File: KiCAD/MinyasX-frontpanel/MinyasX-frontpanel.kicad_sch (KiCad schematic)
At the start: 30 parts, among them J101 Conn_01x04, J102 Conn_02x06_Odd_Even, SW101 SW_Push, SW102 SW_Push, U101 SLG46826G(V2), U102 JOYSTICK, U17 XC6201P332MR-G, U22 PCA9515DP

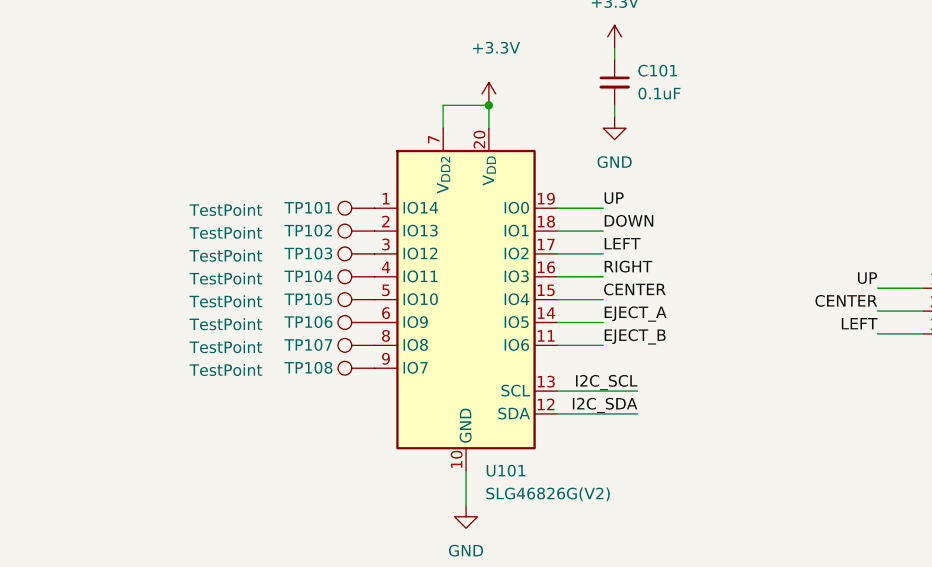
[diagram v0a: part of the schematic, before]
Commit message: * フロントパネルのキー操作ができるようにした * 画面のページ切り替えができるようにした * FDDの回転数とbpsの推定コードを修正した
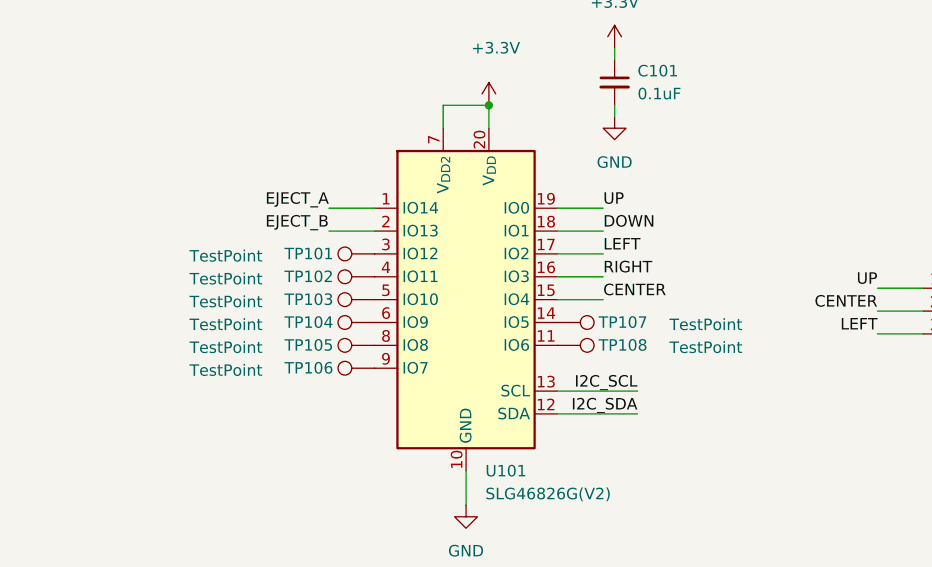
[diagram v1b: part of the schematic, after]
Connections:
- net EJECT_A: now also U101.1 (IO14); no longer U101.14 (IO5)
- net EJECT_B: now also U101.2 (IO13); no longer U101.11 (IO6)
- net at TP106.1: now also U101.9 (IO7); no longer U101.6 (IO9)
- net at TP103.1: now also U101.5 (IO10); no longer U101.3 (IO12)
- net at TP102.1: now also U101.4 (IO11); no longer U101.2 (IO13)
- net at TP107.1: now also U101.14 (IO5); no longer U101.8 (IO8)
- net at TP101.1: now also U101.3 (IO12); no longer U101.1 (IO14)
- net at TP104.1: now also U101.6 (IO9); no longer U101.4 (IO11)
- net at TP105.1: now also U101.8 (IO8); no longer U101.5 (IO10)
- net at TP108.1: now also U101.11 (IO6); no longer U101.9 (IO7)
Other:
- moved on the sheet: TP101, TP102, TP103, TP104, TP105, TP106, TP107, TP108
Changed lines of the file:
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@@
 	(wire
 		(pts
-			(xy 111.76 129.54) (xy 106.68 129.54)
+			(xy 81.28 116.84) (xy 86.36 116.84)
 		)
 		(stroke
@@
 	(wire
 		(pts
-			(xy 111.76 132.08) (xy 106.68 132.08)
+			(xy 81.28 119.38) (xy 86.36 119.38)
 		)
 		(stroke
@@
 	)
 	(label "EJECT_B"
-		(at 111.76 132.08 0)
+		(at 81.28 119.38 180)
 		(effects
 			(font
 				(size 1.27 1.27)
 			)
-			(justify left bottom)
+			(justify right bottom)
 		)
 	)
@@
 	)
 	(label "EJECT_A"
-		(at 111.76 129.54 0)
+		(at 81.28 116.84 180)
 		(effects
 			(font
 				(size 1.27 1.27)
 			)
-			(justify left bottom)
+			(justify right bottom)
 		)
 	)
@@
 	(symbol
 		(lib_id "Connector:TestPoint")
-		(at 86.36 129.54 90)
+		(at 86.36 134.62 90)
 		(unit 1)
 		(exclude_from_sim no)
@@
 		(dnp no)
 		(property "Reference" "TP106"
-			(at 81.788 129.54 90)
+			(at 81.788 134.62 90)
 			(effects
 				(font
@@
 		)
 		(property "Value" "TestPoint"
-			(at 73.914 129.794 90)
+			(at 73.914 134.874 90)
 			(effects
 				(font
@@
 		)
 		(property "Footprint" "TestPoint:TestPoint_Pad_1.0x1.0mm"
-			(at 86.36 124.46 0)
+			(at 86.36 129.54 0)
 			(effects
 				(font
@@
 		)
 		(property "Datasheet" "~"
-			(at 86.36 124.46 0)
+			(at 86.36 129.54 0)
 			(effects
 				(font
@@
 		)
 		(property "Description" "test point"
-			(at 86.36 129.54 0)
+			(at 86.36 134.62 0)
 			(effects
 				(font
@@
 	(symbol
 		(lib_id "Connector:TestPoint")
-		(at 86.36 121.92 90)
+		(at 86.36 127 90)
 		(unit 1)
 		(exclude_from_sim no)
@@
 		(dnp no)
 		(property "Reference" "TP103"
-			(at 81.788 121.92 90)
+			(at 81.788 127 90)
 			(effects
 				(font
@@
 		)
 		(property "Value" "TestPoint"
-			(at 73.914 122.174 90)
+			(at 73.914 127.254 90)
 			(effects
 				(font
@@
 		)
 		(property "Footprint" "TestPoint:TestPoint_Pad_1.0x1.0mm"
-			(at 86.36 116.84 0)
+			(at 86.36 121.92 0)
 			(effects
 				(font
@@
 		)
 		(property "Datasheet" "~"
-			(at 86.36 116.84 0)
+			(at 86.36 121.92 0)
 			(effects
 				(font
@@
 		)
 		(property "Description" "test point"
-			(at 86.36 121.92 0)
+			(at 86.36 127 0)
 			(effects
 				(font
@@
 	(symbol
 		(lib_id "Connector:TestPoint")
-		(at 86.36 119.38 90)
+		(at 86.36 124.46 90)
 		(unit 1)
 		(exclude_from_sim no)
@@
 		(dnp no)
 		(property "Reference" "TP102"
-			(at 81.788 119.38 90)
+			(at 81.788 124.46 90)
 			(effects
 				(font
@@
 		)
 		(property "Value" "TestPoint"
-			(at 73.914 119.634 90)
+			(at 73.914 124.714 90)
 			(effects
 				(font
@@
 		)
 		(property "Footprint" "TestPoint:TestPoint_Pad_1.0x1.0mm"
-			(at 86.36 114.3 0)
+			(at 86.36 119.38 0)
 			(effects
 				(font
@@
 		)
 		(property "Datasheet" "~"
-			(at 86.36 114.3 0)
+			(at 86.36 119.38 0)
 			(effects
 				(font
@@
 		)
 		(property "Description" "test point"
-			(at 86.36 119.38 0)
+			(at 86.36 124.46 0)
 			(effects
 				(font
@@
 	(symbol
 		(lib_id "Connector:TestPoint")
-		(at 86.36 132.08 90)
+		(at 106.68 129.54 270)
+		(mirror x)
 		(unit 1)
 		(exclude_from_sim no)
@@
 		(dnp no)
 		(property "Reference" "TP107"
-			(at 81.788 132.08 90)
+			(at 111.252 129.54 90)
 			(effects
 				(font
@@
 		)
 		(property "Value" "TestPoint"
-			(at 73.914 132.334 90)
+			(at 119.126 129.794 90)
 			(effects
 				(font
@@
 		)
 		(property "Footprint" "TestPoint:TestPoint_Pad_1.0x1.0mm"
-			(at 86.36 127 0)
+			(at 106.68 124.46 0)
 			(effects
 				(font
@@
 		)
 		(property "Datasheet" "~"
-			(at 86.36 127 0)
+			(at 106.68 124.46 0)
 			(effects
 				(font
@@
 		)
 		(property "Description" "test point"
-			(at 86.36 132.08 0)
+			(at 106.68 129.54 0)
 			(effects
 				(font
@@
 	(symbol
 		(lib_id "Connector:TestPoint")
-		(at 86.36 116.84 90)
+		(at 86.36 121.92 90)
 		(unit 1)
 		(exclude_from_sim no)
@@
 		(dnp no)
 		(property "Reference" "TP101"
-			(at 81.788 116.84 90)
+			(at 81.788 121.92 90)
 			(effects
 				(font
@@
 		)
 		(property "Value" "TestPoint"
-			(at 73.914 117.094 90)
+			(at 73.914 122.174 90)
 			(effects
 				(font
@@
 		)
 		(property "Footprint" "TestPoint:TestPoint_Pad_1.0x1.0mm"
-			(at 86.36 111.76 0)
+			(at 86.36 116.84 0)
 			(effects
 				(font
@@
 		)
 		(property "Datasheet" "~"
-			(at 86.36 111.76 0)
+			(at 86.36 116.84 0)
 			(effects
 				(font
@@
 		)
 		(property "Description" "test point"
-			(at 86.36 116.84 0)
+			(at 86.36 121.92 0)
 			(effects
 				(font
@@
 	(symbol
 		(lib_id "Connector:TestPoint")
-		(at 86.36 124.46 90)
+		(at 86.36 129.54 90)
 		(unit 1)
 		(exclude_from_sim no)
@@
 		(dnp no)
 		(property "Reference" "TP104"
-			(at 81.788 124.46 90)
+			(at 81.788 129.54 90)
 			(effects
 				(font
@@
 		)
 		(property "Value" "TestPoint"
-			(at 73.914 124.714 90)
+			(at 73.914 129.794 90)
 			(effects
 				(font
@@
 		)
 		(property "Footprint" "TestPoint:TestPoint_Pad_1.0x1.0mm"
-			(at 86.36 119.38 0)
+			(at 86.36 124.46 0)
 			(effects
 				(font
@@
 		)
 		(property "Datasheet" "~"
-			(at 86.36 119.38 0)
+			(at 86.36 124.46 0)
 			(effects
 				(font
@@
 		)
 		(property "Description" "test point"
-			(at 86.36 124.46 0)
+			(at 86.36 129.54 0)
 			(effects
 				(font
@@
 	(symbol
 		(lib_id "Connector:TestPoint")
-		(at 86.36 134.62 90)
+		(at 106.68 132.08 270)
+		(mirror x)
 		(unit 1)
 		(exclude_from_sim no)
@@
 		(dnp no)
 		(property "Reference" "TP108"
-			(at 81.788 134.62 90)
+			(at 111.252 132.08 90)
 			(effects
 				(font
@@
 		)
 		(property "Value" "TestPoint"
-			(at 73.914 134.874 90)
+			(at 119.126 132.334 90)
 			(effects
 				(font
@@
 		)
 		(property "Footprint" "TestPoint:TestPoint_Pad_1.0x1.0mm"
-			(at 86.36 129.54 0)
+			(at 106.68 127 0)
 			(effects
 				(font
@@
 		)
 		(property "Datasheet" "~"
-			(at 86.36 129.54 0)
+			(at 106.68 127 0)
 			(effects
 				(font
@@
 		)
 		(property "Description" "test point"
-			(at 86.36 134.62 0)
+			(at 106.68 132.08 0)
 			(effects
 				(font
@@
 	(symbol
 		(lib_id "Connector:TestPoint")
-		(at 86.36 127 90)
+		(at 86.36 132.08 90)
 		(unit 1)
 		(exclude_from_sim no)
@@
 		(dnp no)
 		(property "Reference" "TP105"
-			(at 81.788 127 90)
+			(at 81.788 132.08 90)
 			(effects
 				(font
@@
 		)
 		(property "Value" "TestPoint"
-			(at 73.914 127.254 90)
+			(at 73.914 132.334 90)
 			(effects
 				(font
@@
 		)
 		(property "Footprint" "TestPoint:TestPoint_Pad_1.0x1.0mm"
-			(at 86.36 121.92 0)
+			(at 86.36 127 0)
 			(effects
 				(font
@@
 		)
 		(property "Datasheet" "~"
-			(at 86.36 121.92 0)
+			(at 86.36 127 0)
 			(effects
 				(font
@@
 		)
 		(property "Description" "test point"
-			(at 86.36 127 0)
+			(at 86.36 132.08 0)
 			(effects
 				(font

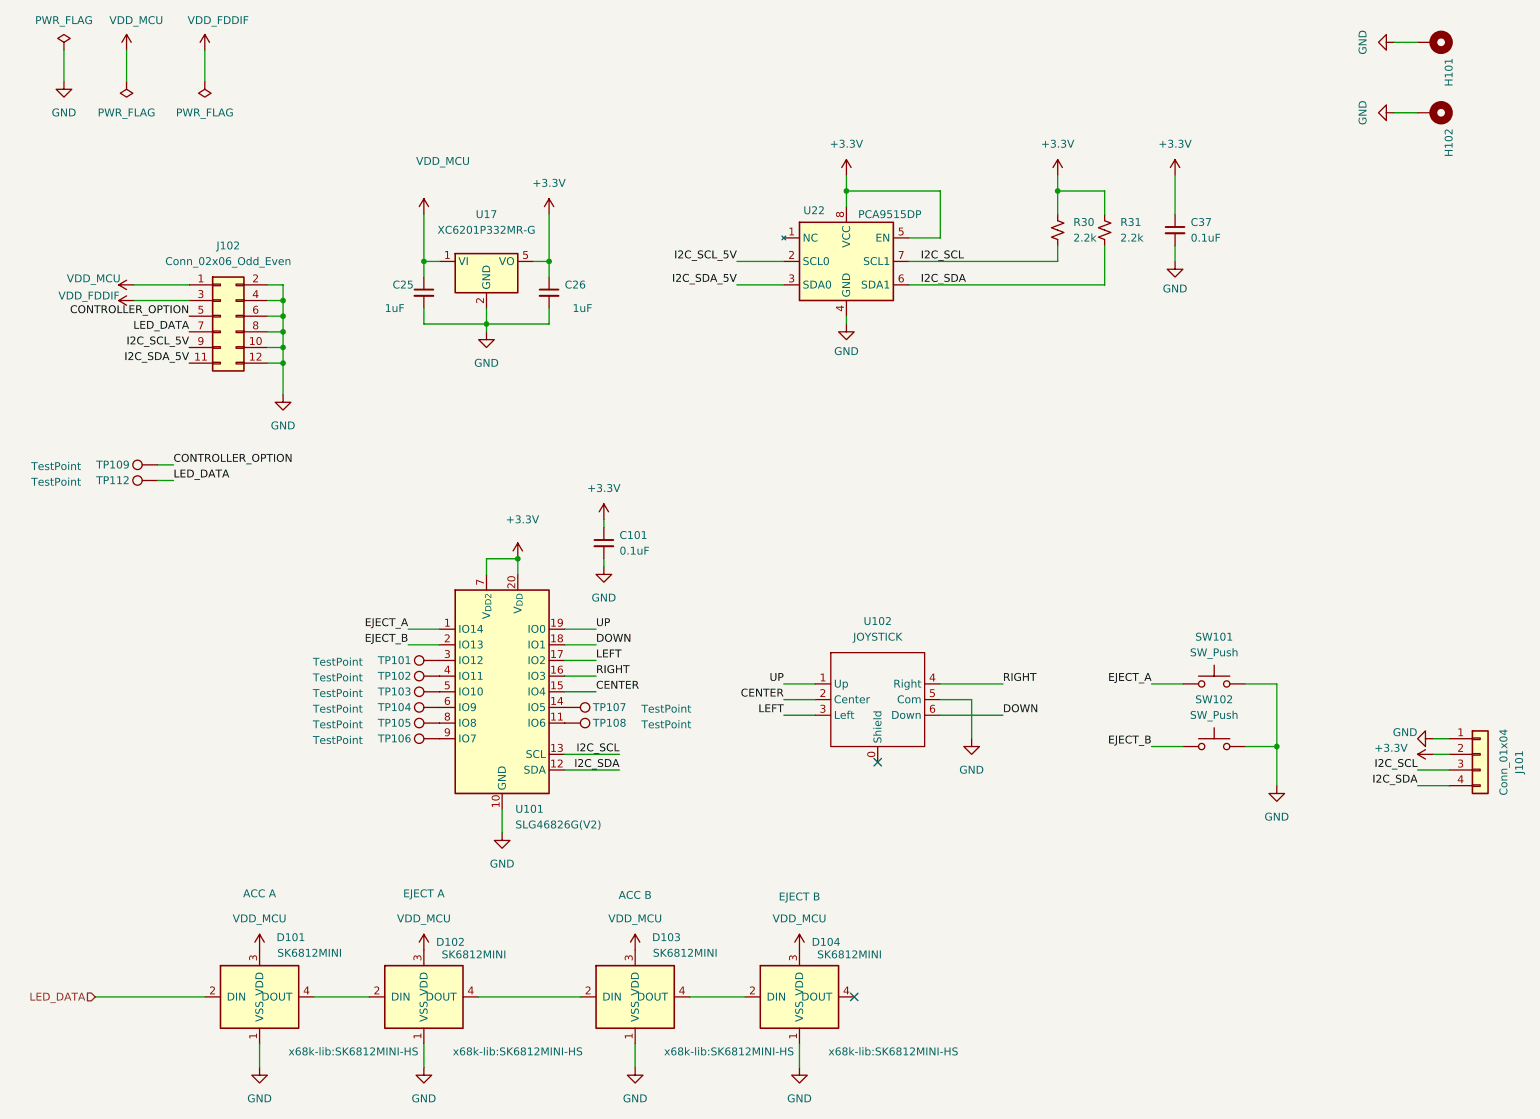
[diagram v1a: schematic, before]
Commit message: フロントパネル周りの配線を見直した
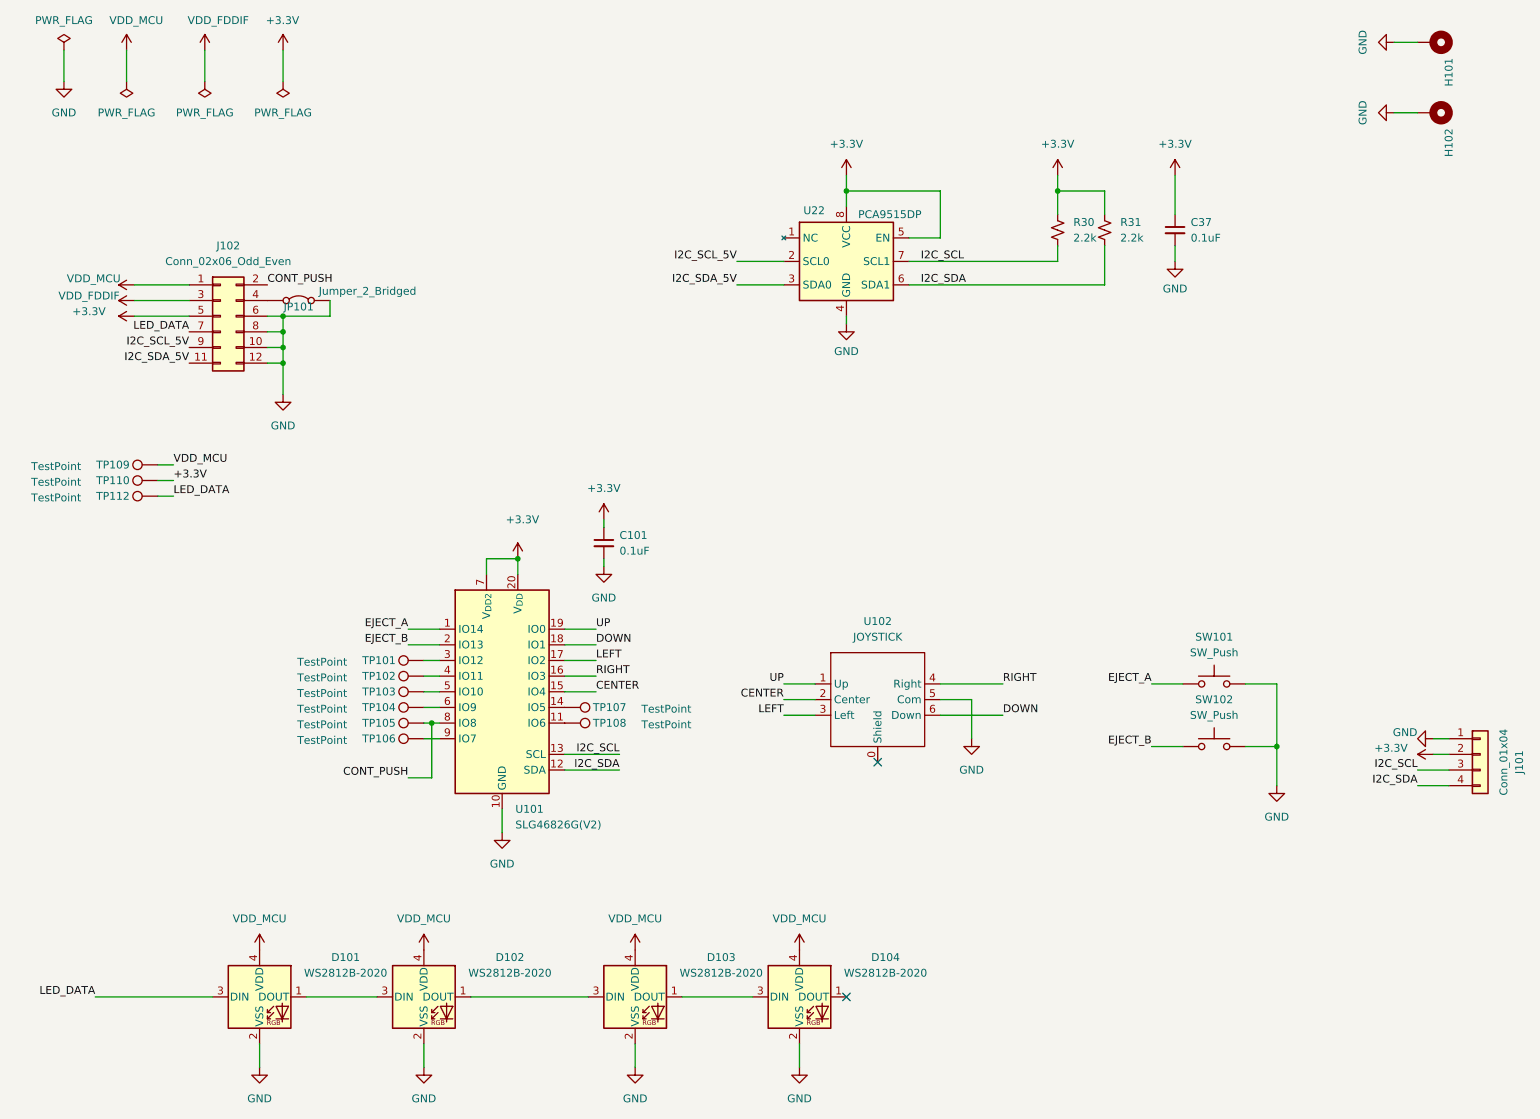
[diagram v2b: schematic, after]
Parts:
- removed C25, C26: 1uF, Capacitor_SMD:C_0603_1608Metric_Pad1.08x0.95mm_HandSolder, symbol Device:C_Small
- removed D101, D102, D103, D104: SK6812MINI, x68k-lib:SK6812MINI-HS, symbol x68000-ext:SK6812MINI-HS
- removed U17: XC6201P332MR-G, Package_TO_SOT_SMD:SOT-23-5_HandSoldering, symbol x68000-ext:XC6201P332MR-G
- added D101, D102, D103, D104: WS2812B-2020, LED_SMD:LED_WS2812B-2020_PLCC4_2.0x2.0mm, symbol LED:WS2812B-2020
- added JP101: Jumper_2_Bridged, Jumper:SolderJumper-2_P1.3mm_Bridged_RoundedPad1.0x1.5mm, symbol Jumper:Jumper_2_Bridged
- added TP110: TestPoint, TestPoint:TestPoint_Pad_1.0x1.0mm, symbol Connector:TestPoint
- U101: LCSC (none) -> C3281959
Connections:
- net +3.3V: now also J102.5 (Pin_5), TP110.1
- net GND: now also D101.2 (VSS), D102.2 (VSS), D103.2 (VSS), D104.2 (VSS), JP101.2 (B); no longer J102.2 (Pin_2), J102.4 (Pin_4)
- net LED_DATA: now also D101.3 (DIN)
- net VDD_MCU: now also TP109.1, D101.4 (VDD), D102.4 (VDD), D103.4 (VDD), D104.4 (VDD)
- net CONT_PUSH: now reaches TP105.1, U101.8 (IO8)
- net CONT_PUSH: now also J102.2 (Pin_2)
- removed net CONTROLLER_OPTION: J102.5 (Pin_5), TP109.1
- new net: D103.1 (DOUT), D104.3 (DIN)
- new net: J102.4 (Pin_4), JP101.1 (A)
- new net: D102.1 (DOUT), D103.3 (DIN)
- new net: D101.1 (DOUT), D102.3 (DIN)
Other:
- moved on the sheet: TP101, TP102, TP103, TP104, TP105, TP106, TP112

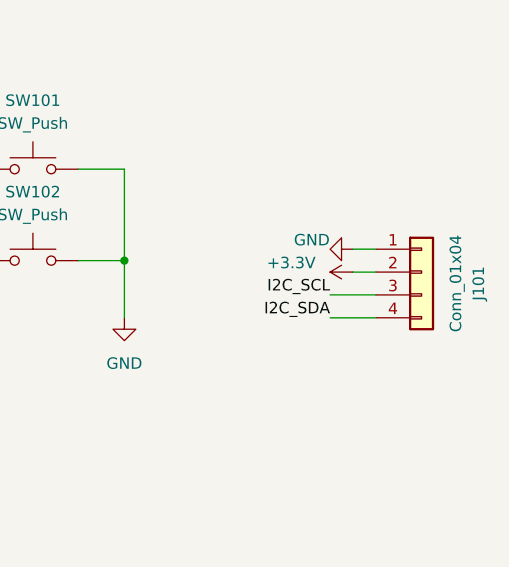
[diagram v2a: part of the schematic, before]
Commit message: PCBA発注のために部品番号などを追加した
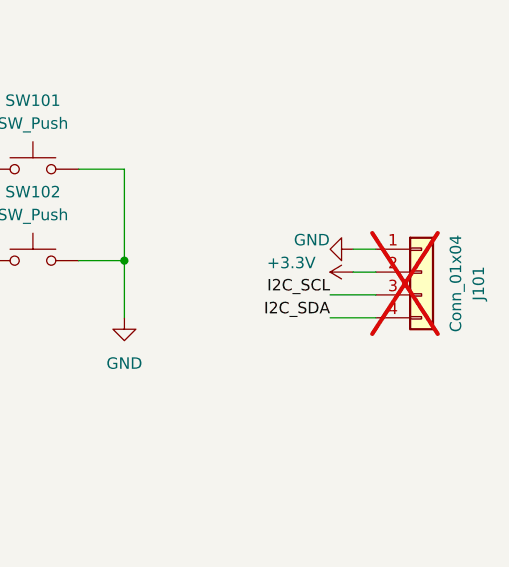
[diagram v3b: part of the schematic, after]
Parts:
- J101: now not fitted
- J102: LCSC (none) -> C492423
- SW101, SW102: LCSC (none) -> C720477
- U102: LCSC (none) -> C202423
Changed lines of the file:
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@@
 			)
 		)
+		(property "LCSC" "C720477"
+			(at 212.09 135.89 0)
+			(effects
+				(font
+					(size 1.27 1.27)
+				)
+				(hide yes)
+			)
+		)
 		(pin "1"
 		)
@@
 		(in_bom yes)
 		(on_board yes)
-		(dnp no)
+		(dnp yes)
 		(fields_autoplaced yes)
 		(property "Reference" "J101"
@@
 			)
 		)
+		(property "LCSC" "C720477"
+			(at 212.09 125.73 0)
+			(effects
+				(font
+					(size 1.27 1.27)
+				)
+				(hide yes)
+			)
+		)
 		(pin "1"
 		)
@@
 			)
 		)
+		(property "LCSC" "C492423"
+			(at 50.8 66.04 0)
+			(effects
+				(font
+					(size 1.27 1.27)
+				)
+				(hide yes)
+			)
+		)
 		(pin "1"
 		)
@@
 			(at 157.48 128.27 0)
 			(effects
+				(font
+					(size 1.27 1.27)
+				)
+				(hide yes)
+			)
+		)
+		(property "LCSC" "C202423"
+			(at 157.48 128.27 0)
+			(effects

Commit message: v2.1.0のPCBA発注
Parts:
- U2002: renamed from U22; LCSC C129512 -> C2652413
- renumbered C101 to C2001, C37 to C2002, D101 to D2001, D102 to D2002, D103 to D2003, D104 to D2004, H101 to H2001, H102 to H2002, J102 to J2001, J101 to J2002, JP101 to JP2001, R30 to R2001, R31 to R2002, SW101 to SW2001, SW102 to SW2002, TP109 to TP2001, TP110 to TP2002, TP112 to TP2003, TP101 to TP2004, TP102 to TP2005, TP103 to TP2006, TP104 to TP2007, TP105 to TP2008, TP106 to TP2009, TP107 to TP2010, TP108 to TP2011, U101 to U2001, U102 to U2003
